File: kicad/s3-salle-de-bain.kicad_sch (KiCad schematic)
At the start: 23 parts, among them J1 Jack 3.5mm switch detect, J2 USB-C 5V input, Q1 P-MOSFET high-side (AO3401), SW1 Encodeur Alps EC11, SW2 Switch mute SPDT, U1 ESP32-S3-DevKitC-1, U2 PCM5102, U3 PAM8403, U4 INMP441 (MEMS I2S), U5 AMS1117-3.3 (LDO)

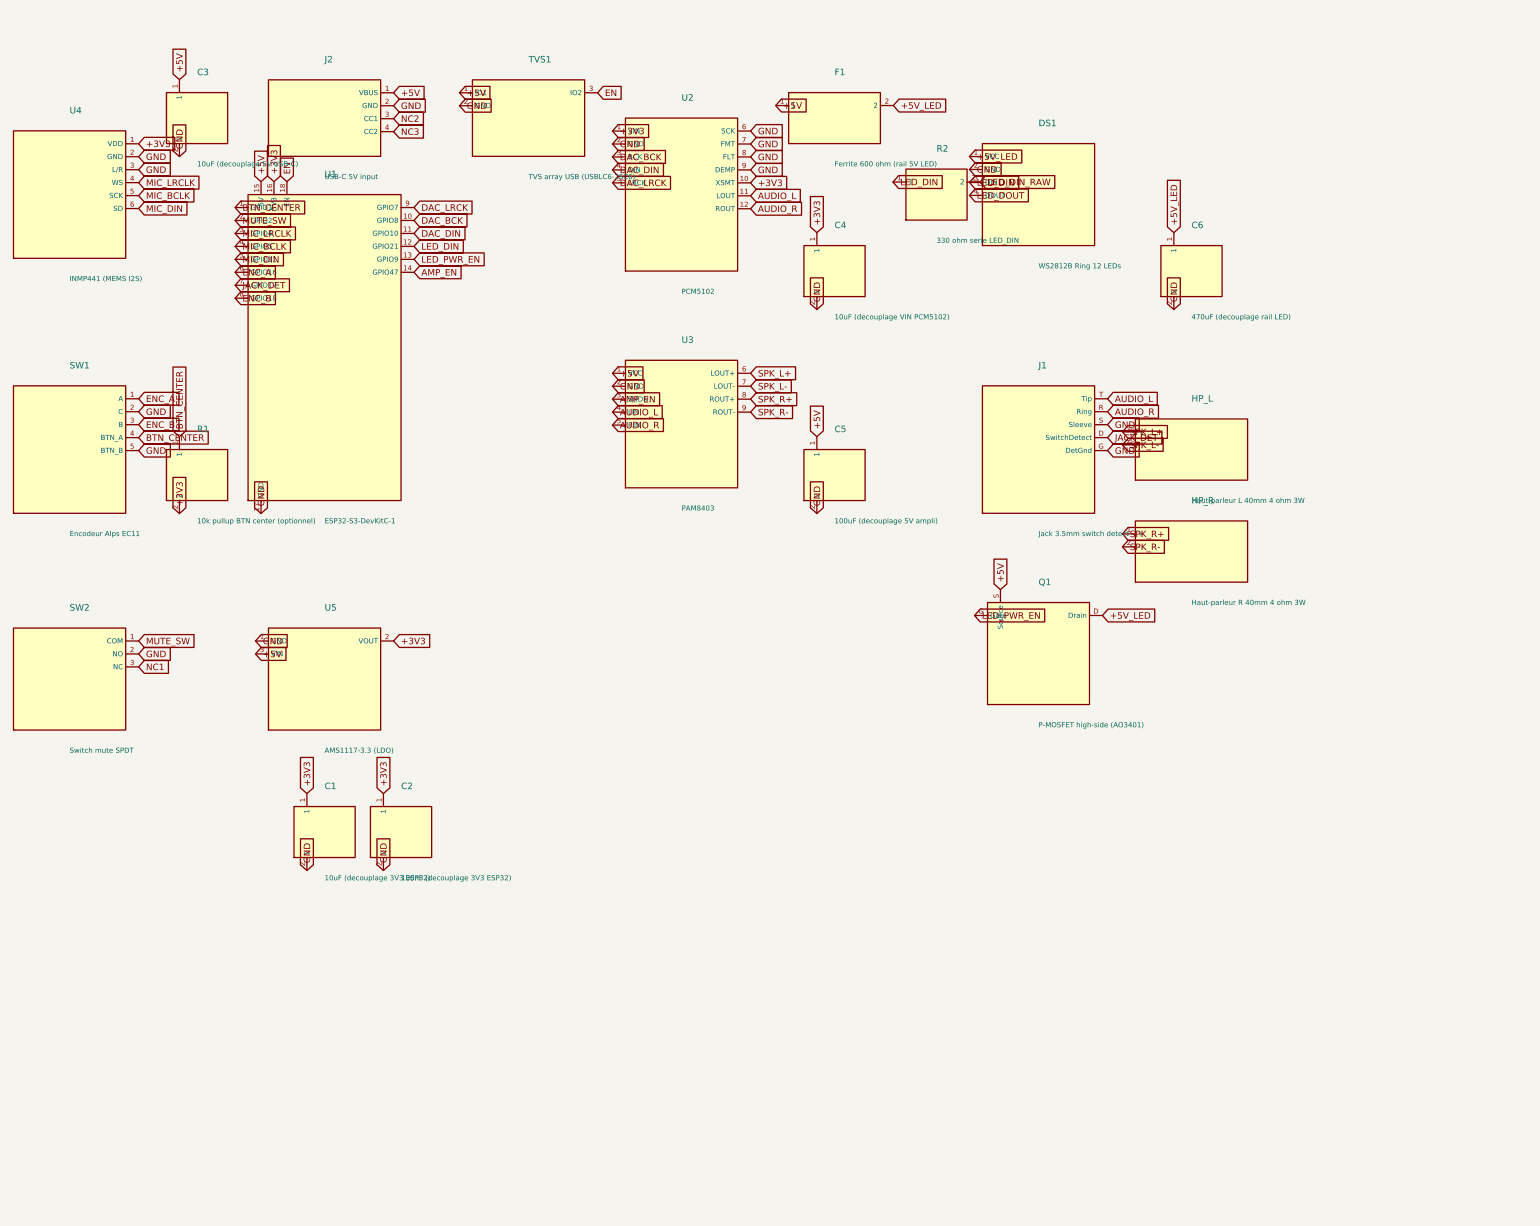
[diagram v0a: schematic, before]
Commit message: fix(kicad): properly wire schematic with 97 wires + 30 junctions, add SVG preview
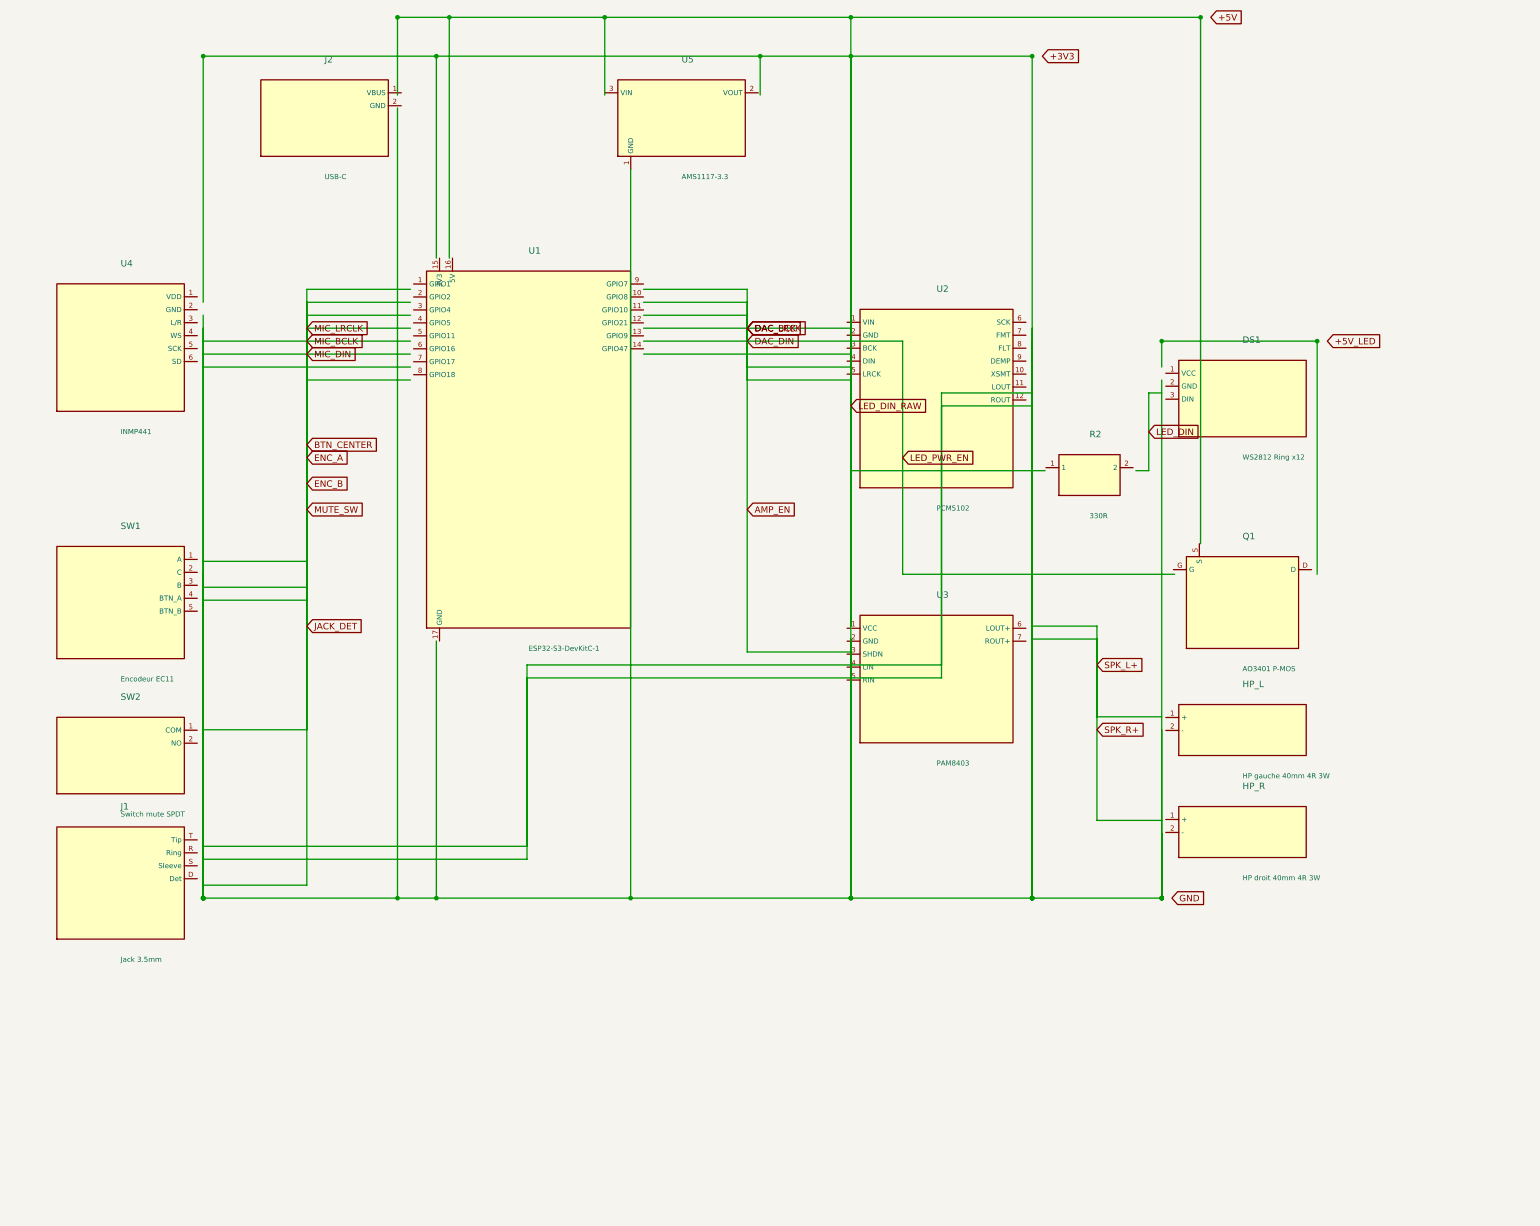
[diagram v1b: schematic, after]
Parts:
- removed C1: 10uF (decouplage 3V3 ESP32), Capacitor_SMD:C_0805_2012Metric, symbol Local:C1
- removed C2: 100nF (decouplage 3V3 ESP32), Capacitor_SMD:C_0603_1608Metric, symbol Local:C2
- removed C3: 10uF (decouplage 5V USB-C), Capacitor_SMD:C_0805_2012Metric, symbol Local:C3
- removed C4: 10uF (decouplage VIN PCM5102), Capacitor_SMD:C_0805_2012Metric, symbol Local:C4
- removed C5: 100uF (decouplage 5V ampli), Capacitor_SMD:CP_Elec_5x5.4, symbol Local:C5
- removed C6: 470uF (decouplage rail LED), Capacitor_SMD:CP_Elec_6.3x5.4, symbol Local:C6
- removed F1: Ferrite 600 ohm (rail 5V LED), Inductor_SMD:L_0603_1608Metric, symbol Local:F1
- removed R1: 10k pullup BTN center (optionnel), Resistor_SMD:R_0603_1608Metric, symbol Local:R1
- removed TVS1: TVS array USB (USBLC6-2SC6), Package_TO_SOT_SMD:SOT-23-6, symbol Local:TVS1
- DS1: value WS2812B Ring 12 LEDs -> WS2812 Ring x12
- HP_L: value Haut-parleur L 40mm 4 ohm 3W -> HP gauche 40mm 4R 3W
- HP_R: value Haut-parleur R 40mm 4 ohm 3W -> HP droit 40mm 4R 3W
- J1: value Jack 3.5mm switch detect -> Jack 3.5mm
- J2: value USB-C 5V input -> USB-C
- Q1: value P-MOSFET high-side (AO3401) -> AO3401 P-MOS
- R2: value 330 ohm serie LED_DIN -> 330R
- SW1: value Encodeur Alps EC11 -> Encodeur EC11
- U4: value INMP441 (MEMS I2S) -> INMP441
- U5: value AMS1117-3.3 (LDO) -> AMS1117-3.3
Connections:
- net +3V3: no longer U1.16 (3V3), U2.1 (VIN), U2.10 (XSMT), U4.1 (VDD), U5.2 (VOUT)
- net +5V: no longer J2.1 (VBUS), Q1.S (Source), U1.15 (5V), U3.1 (VCC), U5.3 (VIN)
- net +5V_LED: no longer DS1.1 (VCC), Q1.D (Drain)
- net AMP_EN: no longer U1.14 (GPIO47), U3.3 (SHDN)
- net BTN_CENTER: no longer SW1.4 (BTN_A), U1.1 (GPIO1)
- net GND: no longer DS1.2 (GND), J1.G (DetGnd), J1.S (Sleeve), J2.2 (GND), SW1.2 (C), SW1.5 (BTN_B), SW2.2 (NO), U1.17 (GND), U2.2 (GND), U2.6 (SCK), U2.7 (FMT), U2.8 (FLT), U2.9 (DEMP), U3.2 (GND), U4.2 (GND), U4.3 (L/R), U5.1 (GND)
- net LED_DIN: no longer DS1.3 (DIN), R2.1, U1.12 (GPIO21)
- net SPK_L+: no longer HP_L.1 (+), U3.6 (LOUT+)
- removed net AUDIO_L: J1.T (Tip), U2.11 (LOUT), U3.4 (LIN)
- removed net AUDIO_R: J1.R (Ring), U2.12 (ROUT), U3.5 (RIN)
- net DAC_BCK: no longer names the net of U1.10 (GPIO8)
- net DAC_BCK: no longer U2.3 (BCK)
- net DAC_DIN: no longer names the net of U1.11 (GPIO10)
- net DAC_DIN: no longer U2.4 (DIN)
- net DAC_LRCK: no longer names the net of U1.9 (GPIO7)
- net DAC_LRCK: no longer U2.5 (LRCK)
- removed net EN: U1.18 (EN)
- net ENC_A: no longer names the net of SW1.1 (A)
- net ENC_A: no longer U1.6 (GPIO16)
- net ENC_B: no longer names the net of SW1.3 (B)
- net ENC_B: no longer U1.8 (GPIO18)
- net JACK_DET: no longer names the net of U1.7 (GPIO17)
- net JACK_DET: no longer J1.D (SwitchDetect)
- net LED_DIN_RAW: no longer names the net of R2.2
- removed net LED_DOUT: DS1.4 (DOUT)
- net LED_PWR_EN: no longer names the net of Q1.G
- net LED_PWR_EN: no longer U1.13 (GPIO9)
- net MIC_BCLK: no longer names the net of U4.5 (SCK)
- net MIC_BCLK: no longer U1.4 (GPIO5)
- net MIC_DIN: no longer names the net of U4.6 (SD)
- net MIC_DIN: no longer U1.5 (GPIO11)
- net MIC_LRCLK: no longer names the net of U4.4 (WS)
- net MIC_LRCLK: no longer U1.3 (GPIO4)
- net MUTE_SW: no longer names the net of U1.2 (GPIO2)
- net MUTE_SW: no longer SW2.1 (COM)
- removed net NC1: SW2.3 (NC)
- removed net NC2: J2.3 (CC1)
- removed net NC3: J2.4 (CC2)
- net SPK_L-: no longer names the net of U3.7 (ROUT+)
- net SPK_L-: no longer HP_L.2 (-)
- net SPK_R+: no longer names the net of HP_R.1 (+)
- net SPK_R+: no longer U3.8 (ROUT+)
- net SPK_R-: no longer names the net of HP_R.2 (-)
- net SPK_R-: no longer U3.9 (ROUT-)

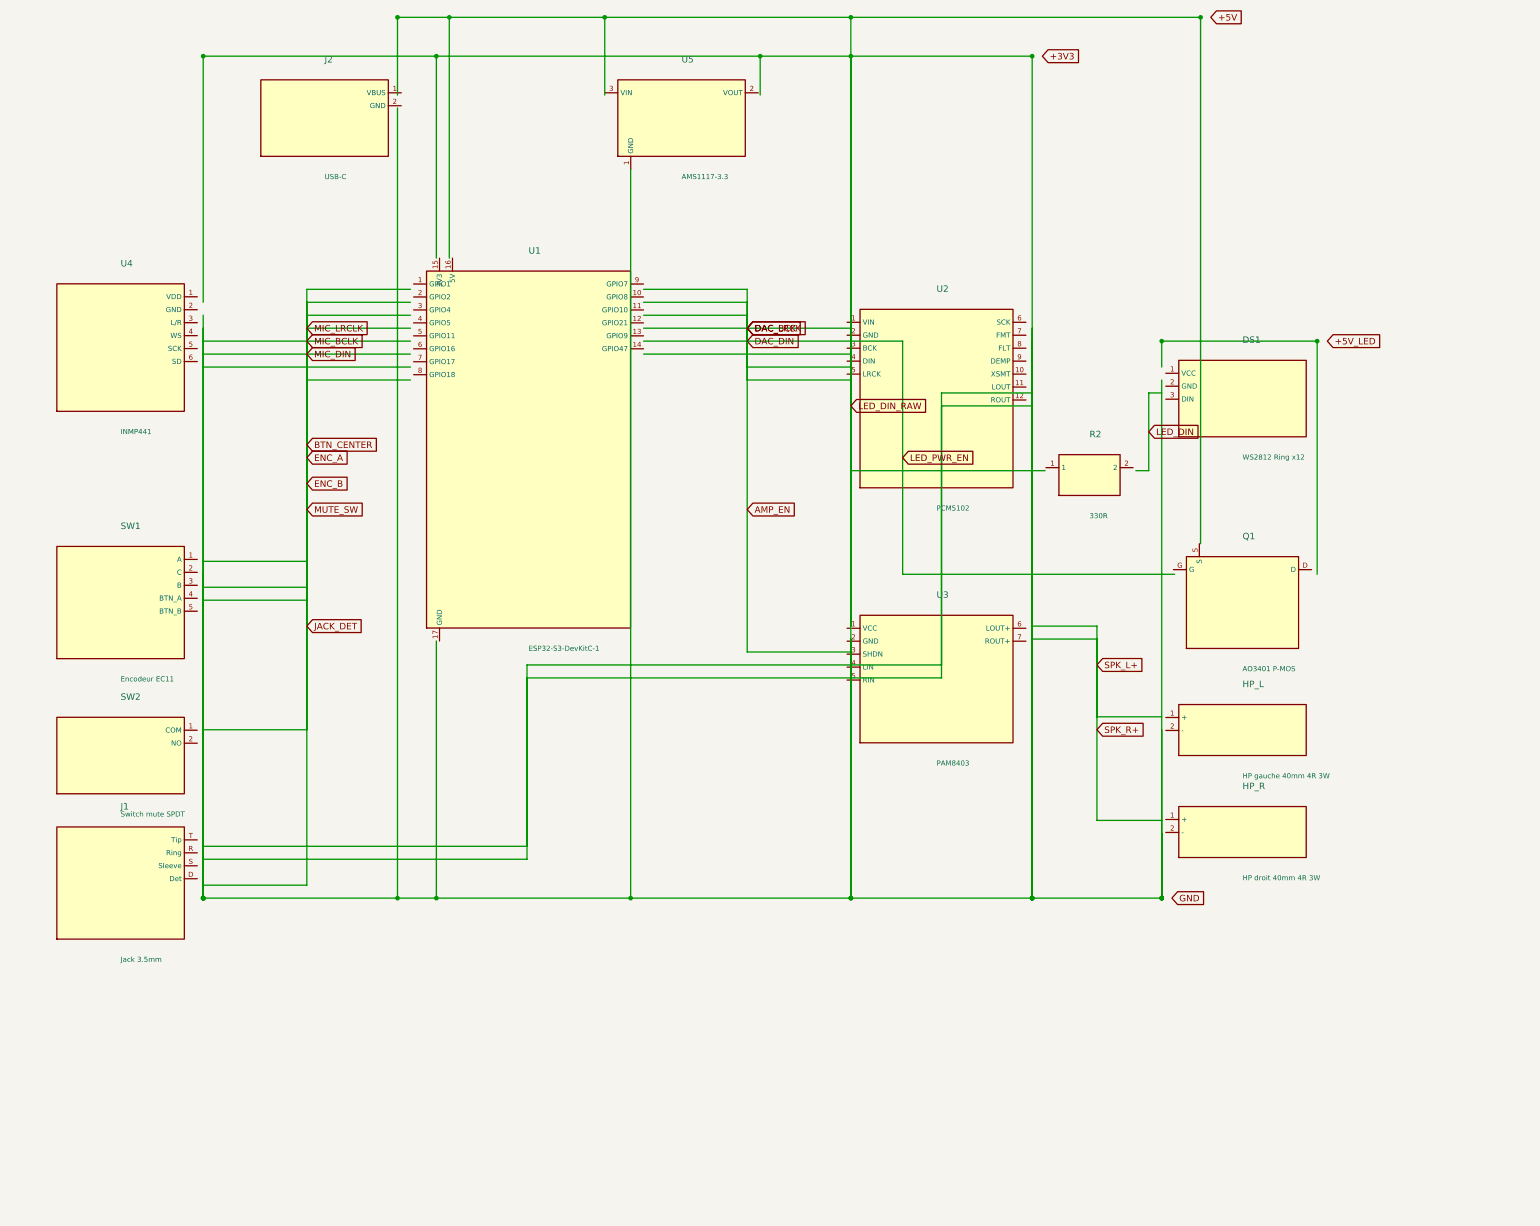
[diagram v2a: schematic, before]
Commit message: feat(kicad): real KiCad standard symbols (Device:R, Device:C, power:GND, Q_PMOS_GSD, Speaker, SW_SPDT)
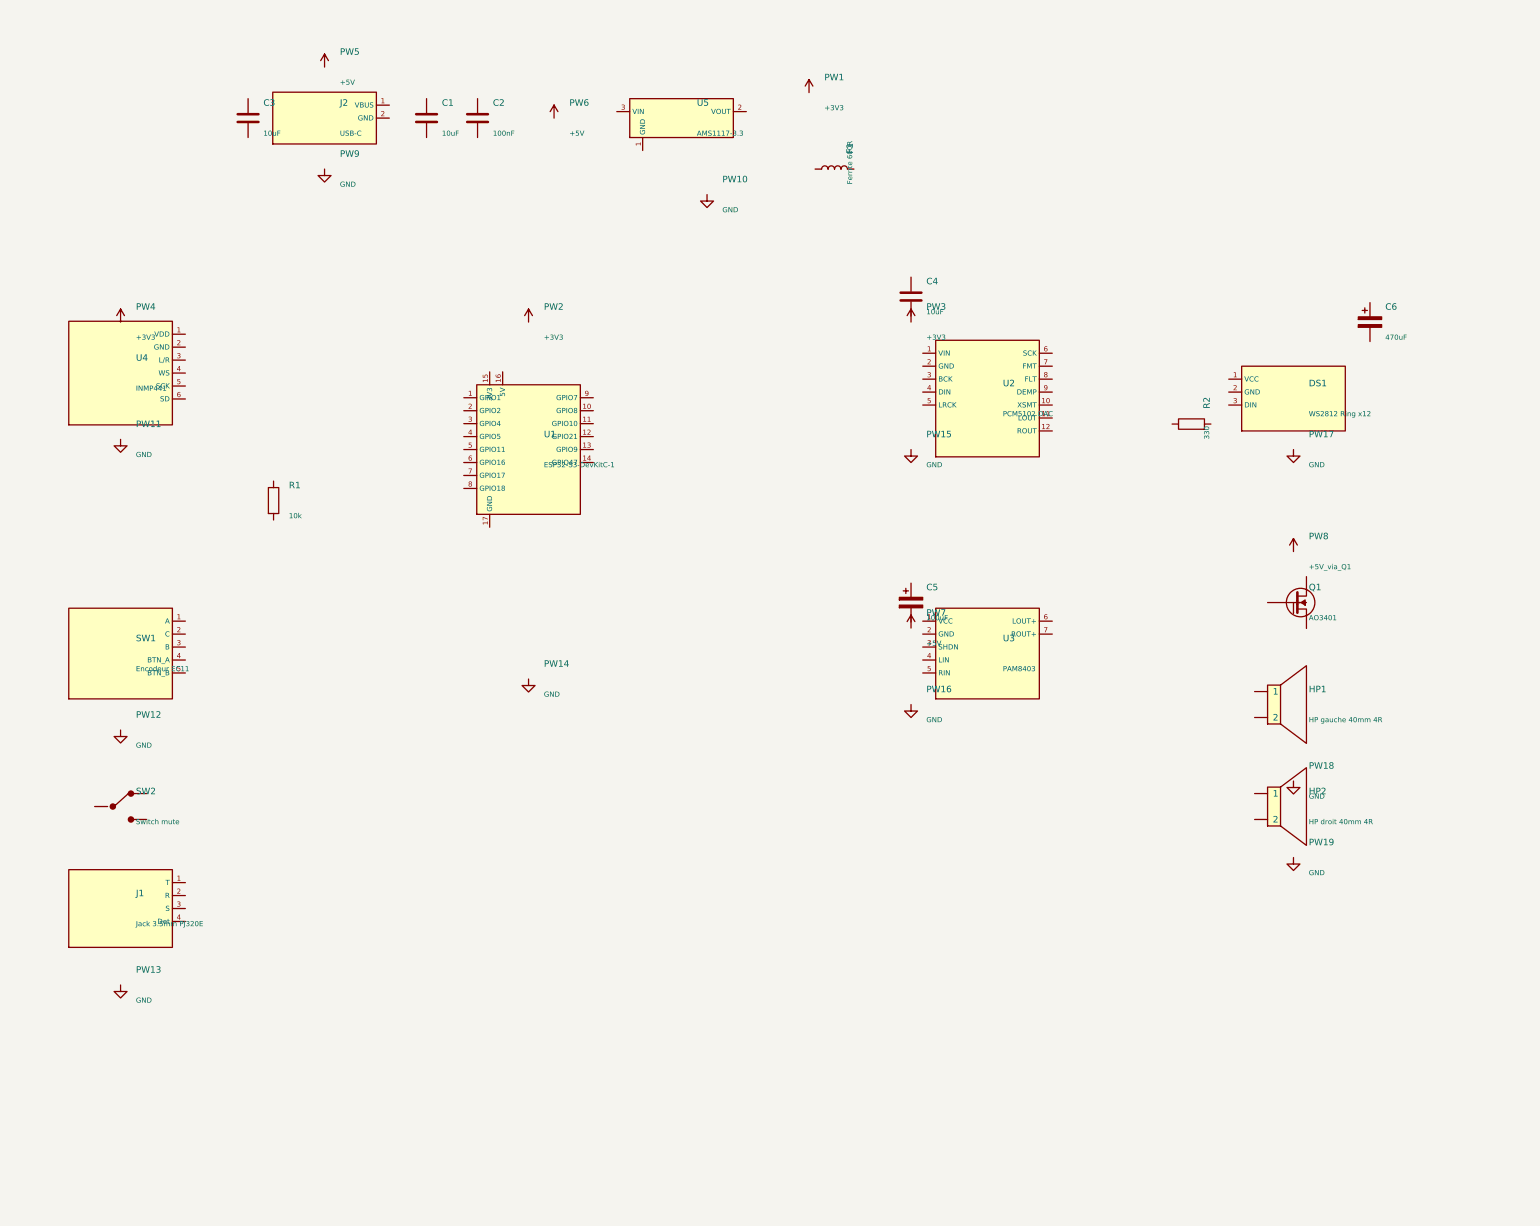
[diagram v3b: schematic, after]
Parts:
- removed DS1: WS2812 Ring x12, Connector_PinHeader_2.54mm:PinHeader_1x04_P2.54mm_Vertical, symbol Local:DS1
- removed HP_L: HP gauche 40mm 4R 3W, Connector_PinHeader_2.54mm:PinHeader_1x02_P2.54mm_Vertical, symbol Local:HP_L
- removed HP_R: HP droit 40mm 4R 3W, Connector_PinHeader_2.54mm:PinHeader_1x02_P2.54mm_Vertical, symbol Local:HP_R
- removed J1: Jack 3.5mm, Connector_Audio:Jack_3.5mm_PJ320E_Vertical, symbol Local:J1
- removed J2: USB-C, Connector_USB:USB_C_Receptacle_USB2.0_16P, symbol Local:J2
- removed Q1: AO3401 P-MOS, Package_TO_SOT_SMD:SOT-23, symbol Local:Q1
- removed R2: 330R, Resistor_SMD:R_0603_1608Metric, symbol Local:R2
- removed SW1: Encodeur EC11, Connector_PinHeader_2.54mm:PinHeader_1x05_P2.54mm_Vertical, symbol Local:SW1
- removed SW2: Switch mute SPDT, Connector_PinHeader_2.54mm:PinHeader_1x03_P2.54mm_Vertical, symbol Local:SW2
- removed U1: ESP32-S3-DevKitC-1, Module:ESP32-S3-DevKitC-1, symbol Local:U1
- removed U2: PCM5102, Connector_PinHeader_2.54mm:PinHeader_2x05_P2.54mm_Vertical, symbol Local:U2
- removed U3: PAM8403, Connector_PinHeader_2.54mm:PinHeader_2x04_P2.54mm_Vertical, symbol Local:U3
- removed U4: INMP441, Connector_PinHeader_2.54mm:PinHeader_1x06_P2.54mm_Vertical, symbol Local:U4
- removed U5: AMS1117-3.3, Package_TO_SOT_SMD:SOT-223-3_TabPin2, symbol Local:U5
- added C1, C3, C4: 10uF, symbol Device:C
- added C2: 100nF, symbol Device:C
- added C5: 100uF, symbol Device:CP
- added C6: 470uF, symbol Device:CP
- added DS1: WS2812 Ring x12, symbol Local:WS2812-Ring
- added F1: Ferrite 600R, symbol Device:L
- added HP1: HP gauche 40mm 4R, symbol Device:Speaker
- added HP2: HP droit 40mm 4R, symbol Device:Speaker
- added J1: Jack 3.5mm PJ320E, symbol Local:Jack-3.5mm
- added J2: USB-C, symbol Local:USB-C
- added Q1: AO3401, symbol Device:Q_PMOS_GSD
- added R1: 10k, symbol Device:R
- added R2: 330, symbol Device:R
- added SW1: Encodeur EC11, symbol Local:EC11-Encoder
- added SW2: Switch mute, symbol Switch:SW_SPDT
- added U1: ESP32-S3-DevKitC-1, symbol Local:ESP32-S3
- added U2: PCM5102 DAC, symbol Local:PCM5102
- added U3: PAM8403, symbol Local:PAM8403
- added U4: INMP441, symbol Local:INMP441
- added U5: AMS1117-3.3, symbol Local:AMS1117-3.3
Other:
- company: domokami / Hanafi BENMESBAH -> domokami / hanafi09
